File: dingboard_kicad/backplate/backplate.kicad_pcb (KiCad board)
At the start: 2 copper layers, 20.3 x 8.4 mm, 2 parts, among them J1 10018784-10210TLF, J2 Bus_PCI_Express_x1

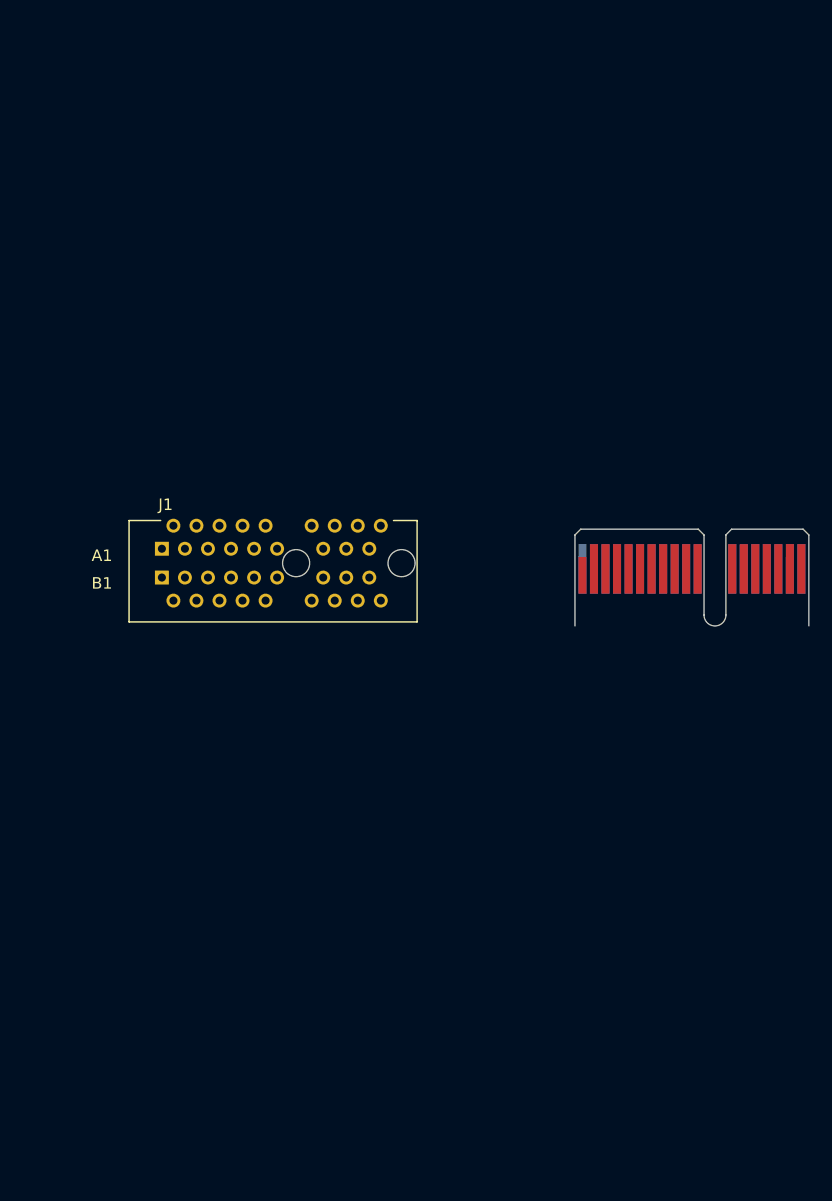
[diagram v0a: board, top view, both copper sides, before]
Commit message: place BME680 in dingboard sensors schematic
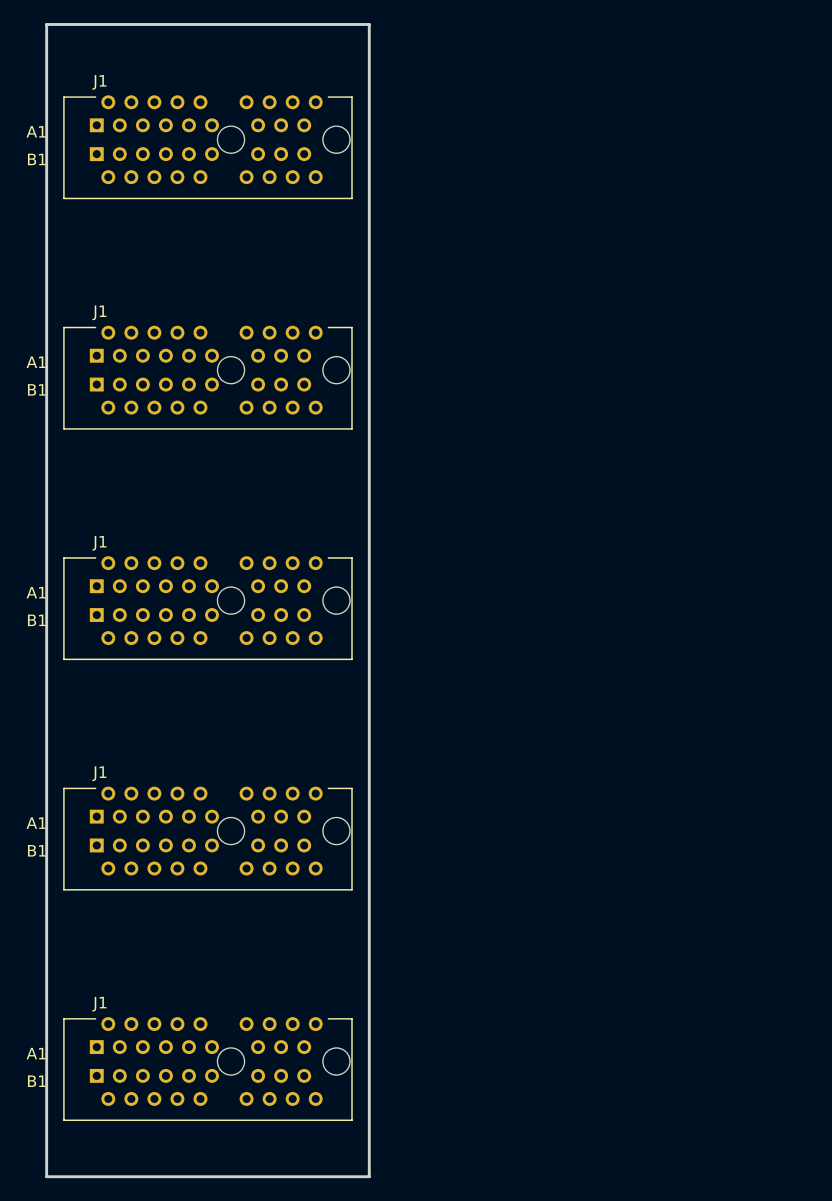
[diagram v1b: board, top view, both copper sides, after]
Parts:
- removed J2: Bus_PCI_Express_x1, Connector_PCBEdge:BUS_PCIexpress_x1
- added J1: 10018784-10210TLF, 10018784_10210TLF:AMPHENOL_10018784-10210TLF, F.Cu at (138.0, 140.0)
- added J1: 10018784-10210TLF, 10018784_10210TLF:AMPHENOL_10018784-10210TLF, F.Cu at (138.0, 60.0)
- added J1: 10018784-10210TLF, 10018784_10210TLF:AMPHENOL_10018784-10210TLF, F.Cu at (138.0, 80.0)
- added J1: 10018784-10210TLF, 10018784_10210TLF:AMPHENOL_10018784-10210TLF, F.Cu at (138.0, 120.0)
- moved J1 6.52 mm to (138.0, 100.0)
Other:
- board size 20.3 x 8.4 mm -> 28 x 100 mm
